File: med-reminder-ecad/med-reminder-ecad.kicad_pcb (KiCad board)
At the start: 2 copper layers, 34 parts, among them J1 USB_B_Micro, J2 22-03-5035, J3 22-03-5025, J4 22-03-5065, Q1 2N3904, Q2 2N3904, Q3 2N3904, Q4 2N3904, U1 LM1117-3.3, U2 QRD1113GR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

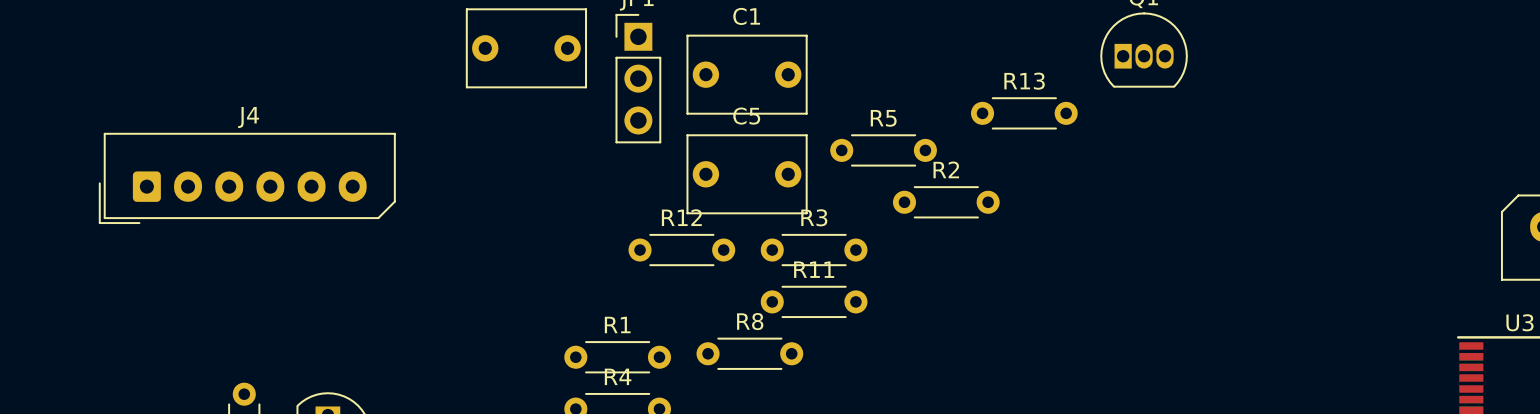
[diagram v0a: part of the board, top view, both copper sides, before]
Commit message: Removed oscillator circuit
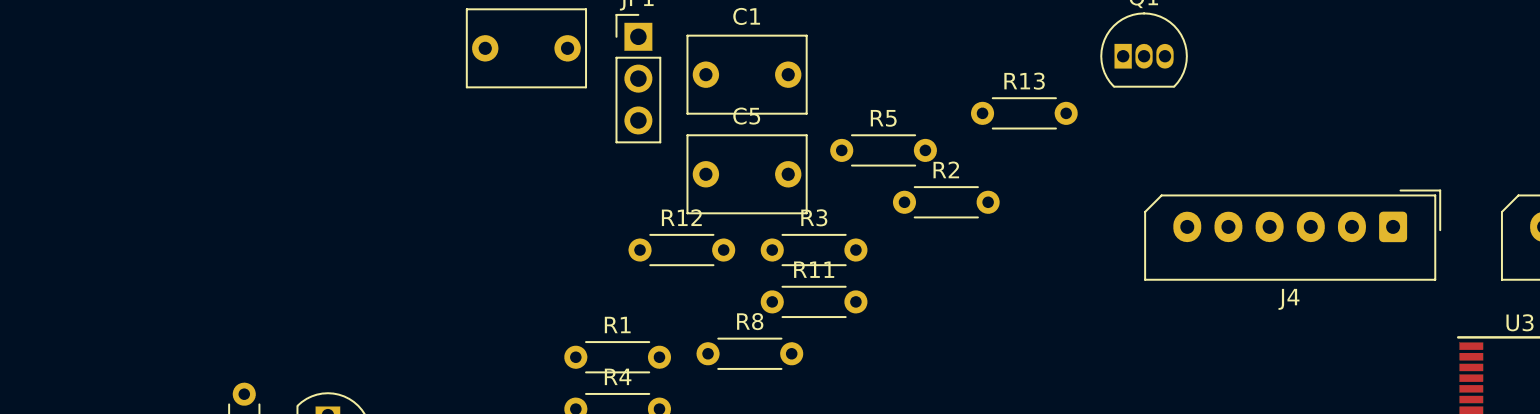
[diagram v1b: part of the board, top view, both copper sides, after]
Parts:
- moved J4 75.7 mm to (201.8, 87.6), turned to 180 degrees
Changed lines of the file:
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@@
     (add_net "Net-(D1-Pad2)")
     (add_net "Net-(D1-Pad3)")
-    (add_net "Net-(J1-Pad4)")
-    (add_net "Net-(J1-Pad6)")
-    (add_net "Net-(J4-Pad6)")
     (add_net "Net-(JP1-Pad2)")
     (add_net "Net-(Q1-Pad2)")
@@
     (add_net "Net-(R11-Pad1)")
     (add_net "Net-(R13-Pad1)")
-    (add_net "Net-(U3-Pad14)")
-    (add_net "Net-(U3-Pad6)")
   )
   (module Capacitor_Tantalum_SMD:CP_EIA-3216-10_Kemet-I (layer F.Cu)
@@
   )
   (module Connector_Molex:Molex_SPOX_5267-06A_1x06_P2.50mm_Vertical (layer F.Cu)
-    (at 126.165001 85.185001)
+    (at 201.85 87.63 180)
     (descr "Molex SPOX Connector System, 5267-06A, 6 Pins per row (http://www.molex.com/pdm_docs/sd/022035035_sd.pdf), generated with kicad-footprint-generator")
     (tags "connector Molex SPOX side entry")
@@
     (fp_line (start -2.45 1.8) (end 13.95 1.8) (layer F.Fab) (width 0.1))
     (fp_line (start -2.45 -3.1) (end -2.45 1.8) (layer F.Fab) (width 0.1))
-    (pad 6 thru_hole oval (at 12.5 0) (size 1.7 1.85) (drill 0.85) (layers *.Cu *.Mask))
-    (pad 5 thru_hole oval (at 10 0) (size 1.7 1.85) (drill 0.85) (layers *.Cu *.Mask)
+    (pad 6 thru_hole oval (at 12.5 0 180) (size 1.7 1.85) (drill 0.85) (layers *.Cu *.Mask))
+    (pad 5 thru_hole oval (at 10 0 180) (size 1.7 1.85) (drill 0.85) (layers *.Cu *.Mask)
       (net 7 /NRST))
-    (pad 4 thru_hole oval (at 7.5 0) (size 1.7 1.85) (drill 0.85) (layers *.Cu *.Mask)
+    (pad 4 thru_hole oval (at 7.5 0 180) (size 1.7 1.85) (drill 0.85) (layers *.Cu *.Mask)
       (net 15 /SWDIO))
-    (pad 3 thru_hole oval (at 5 0) (size 1.7 1.85) (drill 0.85) (layers *.Cu *.Mask)
-      (net 3 GND))
-    (pad 2 thru_hole oval (at 2.5 0) (size 1.7 1.85) (drill 0.85) (layers *.Cu *.Mask)
+    (pad 3 thru_hole oval (at 5 0 180) (size 1.7 1.85) (drill 0.85) (layers *.Cu *.Mask)
+      (net 3 GND))
+    (pad 2 thru_hole oval (at 2.5 0 180) (size 1.7 1.85) (drill 0.85) (layers *.Cu *.Mask)
       (net 16 /SWCLK))
-    (pad 1 thru_hole roundrect (at 0 0) (size 1.7 1.85) (drill 0.85) (layers *.Cu *.Mask) (roundrect_rratio 0.147059)
+    (pad 1 thru_hole roundrect (at 0 0 180) (size 1.7 1.85) (drill 0.85) (layers *.Cu *.Mask) (roundrect_rratio 0.147059)
       (net 4 +3V3))
     (model ${KISYS3DMOD}/Connector_Molex.3dshapes/Molex_SPOX_5267-06A_1x06_P2.50mm_Vertical.wrl
